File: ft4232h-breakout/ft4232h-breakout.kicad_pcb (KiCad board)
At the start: 2 copper layers, 64.1 x 47 mm, 18 parts, among them J1 Conn_01x03, J2 Conn_01x03, J3 Conn_01x03, J4 Conn_01x03, J5 Conn_02x05_SWD, J6 Conn_01x07, J7 Conn_01x07, J8 Conn_01x06, J9 Conn_01x02, X1 FT4232H-MODULE

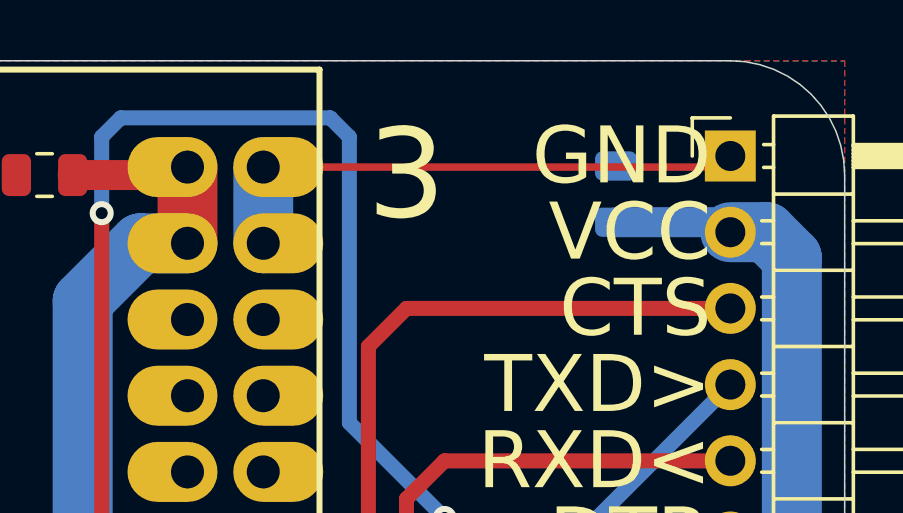
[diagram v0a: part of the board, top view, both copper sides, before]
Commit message: ft4232h-breakout: Jun2021a release, add power led
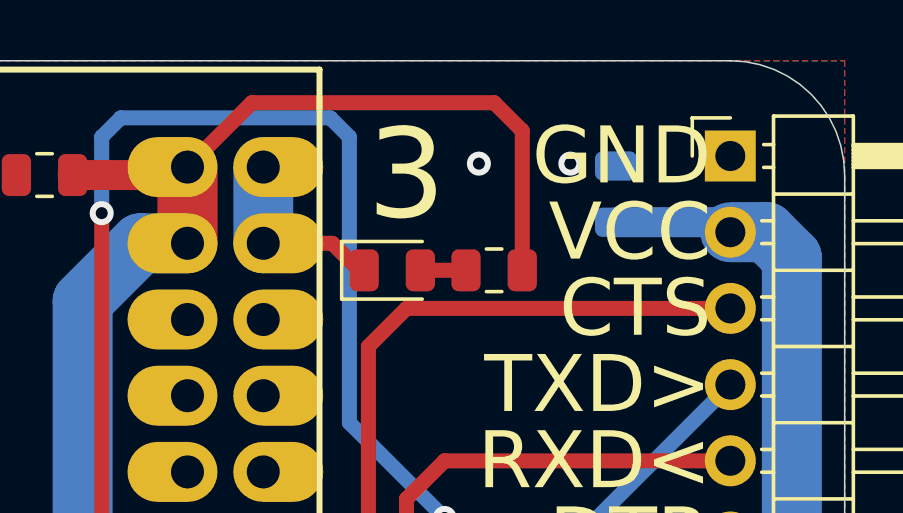
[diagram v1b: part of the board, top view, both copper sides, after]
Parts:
- added D1: LED, tom-opto:LED_0805_2012Metric, F.Cu at (117.0, 88.9)
- added R2: 1k, tom-passives:R_0805_2012Metric, F.Cu at (120.4, 88.9)
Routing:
- net +5V: track 83.2 -> 100.2 mm
- net GND: track 30.9 -> 19.3 mm, vias 3 -> 5
- net Net-(D1-Pad2): track 0.00 -> 1.68 mm

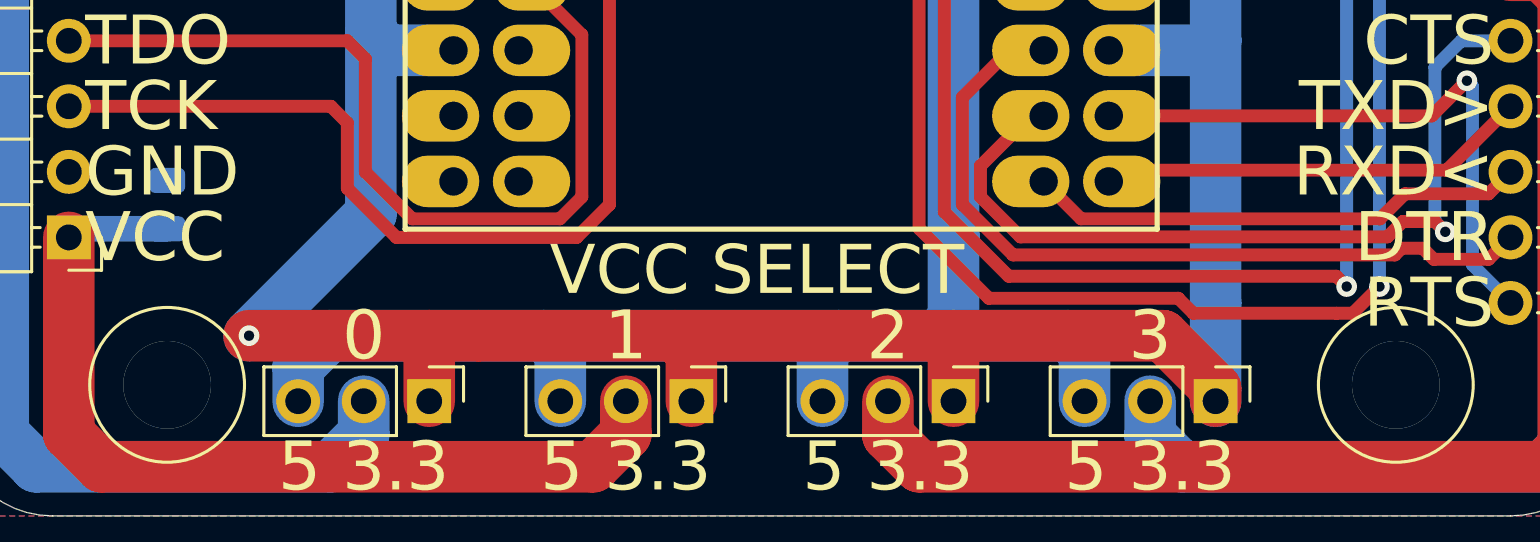
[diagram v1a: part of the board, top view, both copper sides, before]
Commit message: ft4232h-breakout: Jun2021b add silk to voltage selection
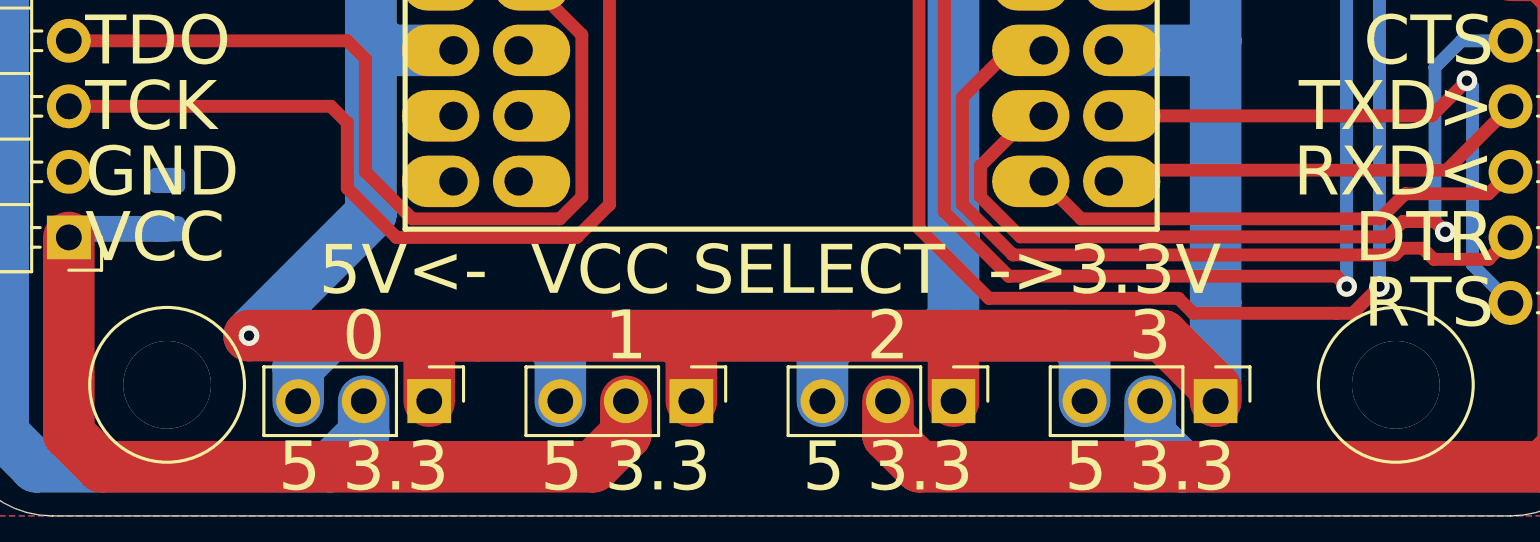
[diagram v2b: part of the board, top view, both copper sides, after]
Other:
- board text added: "5V<- VCC SELECT ->3.3V"
- board text removed: "VCC SELECT"
